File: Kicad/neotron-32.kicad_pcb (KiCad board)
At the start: 2 copper layers, 191.5 x 166.3 mm, 116 parts, among them J1001 2x3 Header, J1002 1x3 UART Debug Header, J1003 Double-mini-DIN-6, J1004 AVR-ISP-6, J101 Conn_02x06, J102 Conn_02x06, J103 Conn_02x04, J1101 DE9 Male, J1201 DE9 Male, J201 DIN-5 180 degree, J202 DIN-5 180 degree, J301 3.5mm Audio Jack TRS, J302 Conn_01x03_Male, J401 USB_B, J501 SD_Card, J601 Conn_02x13_Header, J801 DB15HD_Female, J901 Conn_02x05, SW1001 SW_Push_DPDT_ON_MO, SW401 SW_Push_DPDT_ON_MO, U1001 MCP23017_SP, U1002 ATmega328P-PU, U101 EK-TM4C123GXL, U201 74LS14, U202 6N138, U401 MIC2005A-2YM5, U402 TC1262-33, U601 MCP23S17_SP, U701 MCP7940N-xP, U901 ICL3232CPZMAX, Y701 32,768 Hz

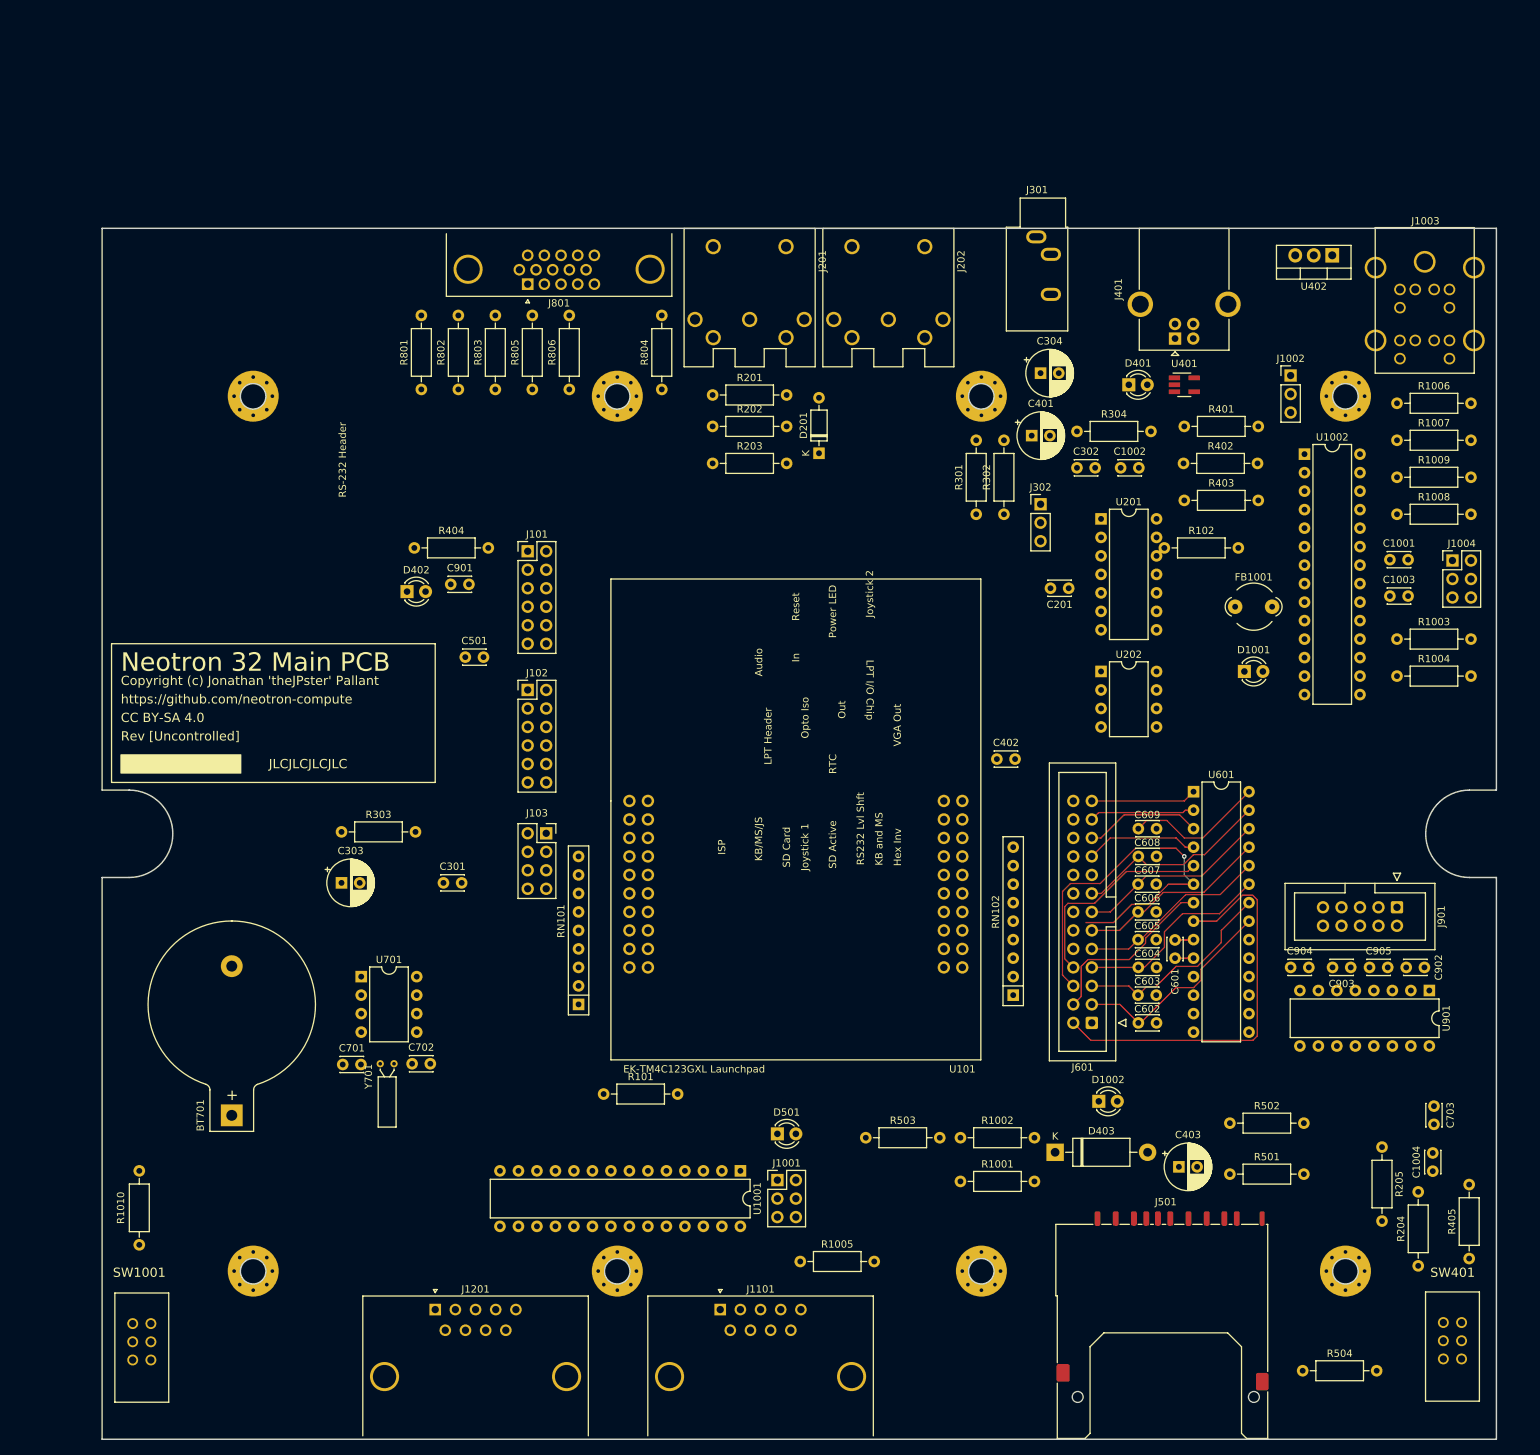
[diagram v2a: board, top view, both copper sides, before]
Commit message: Moved Joystick controller onto its own sheet.
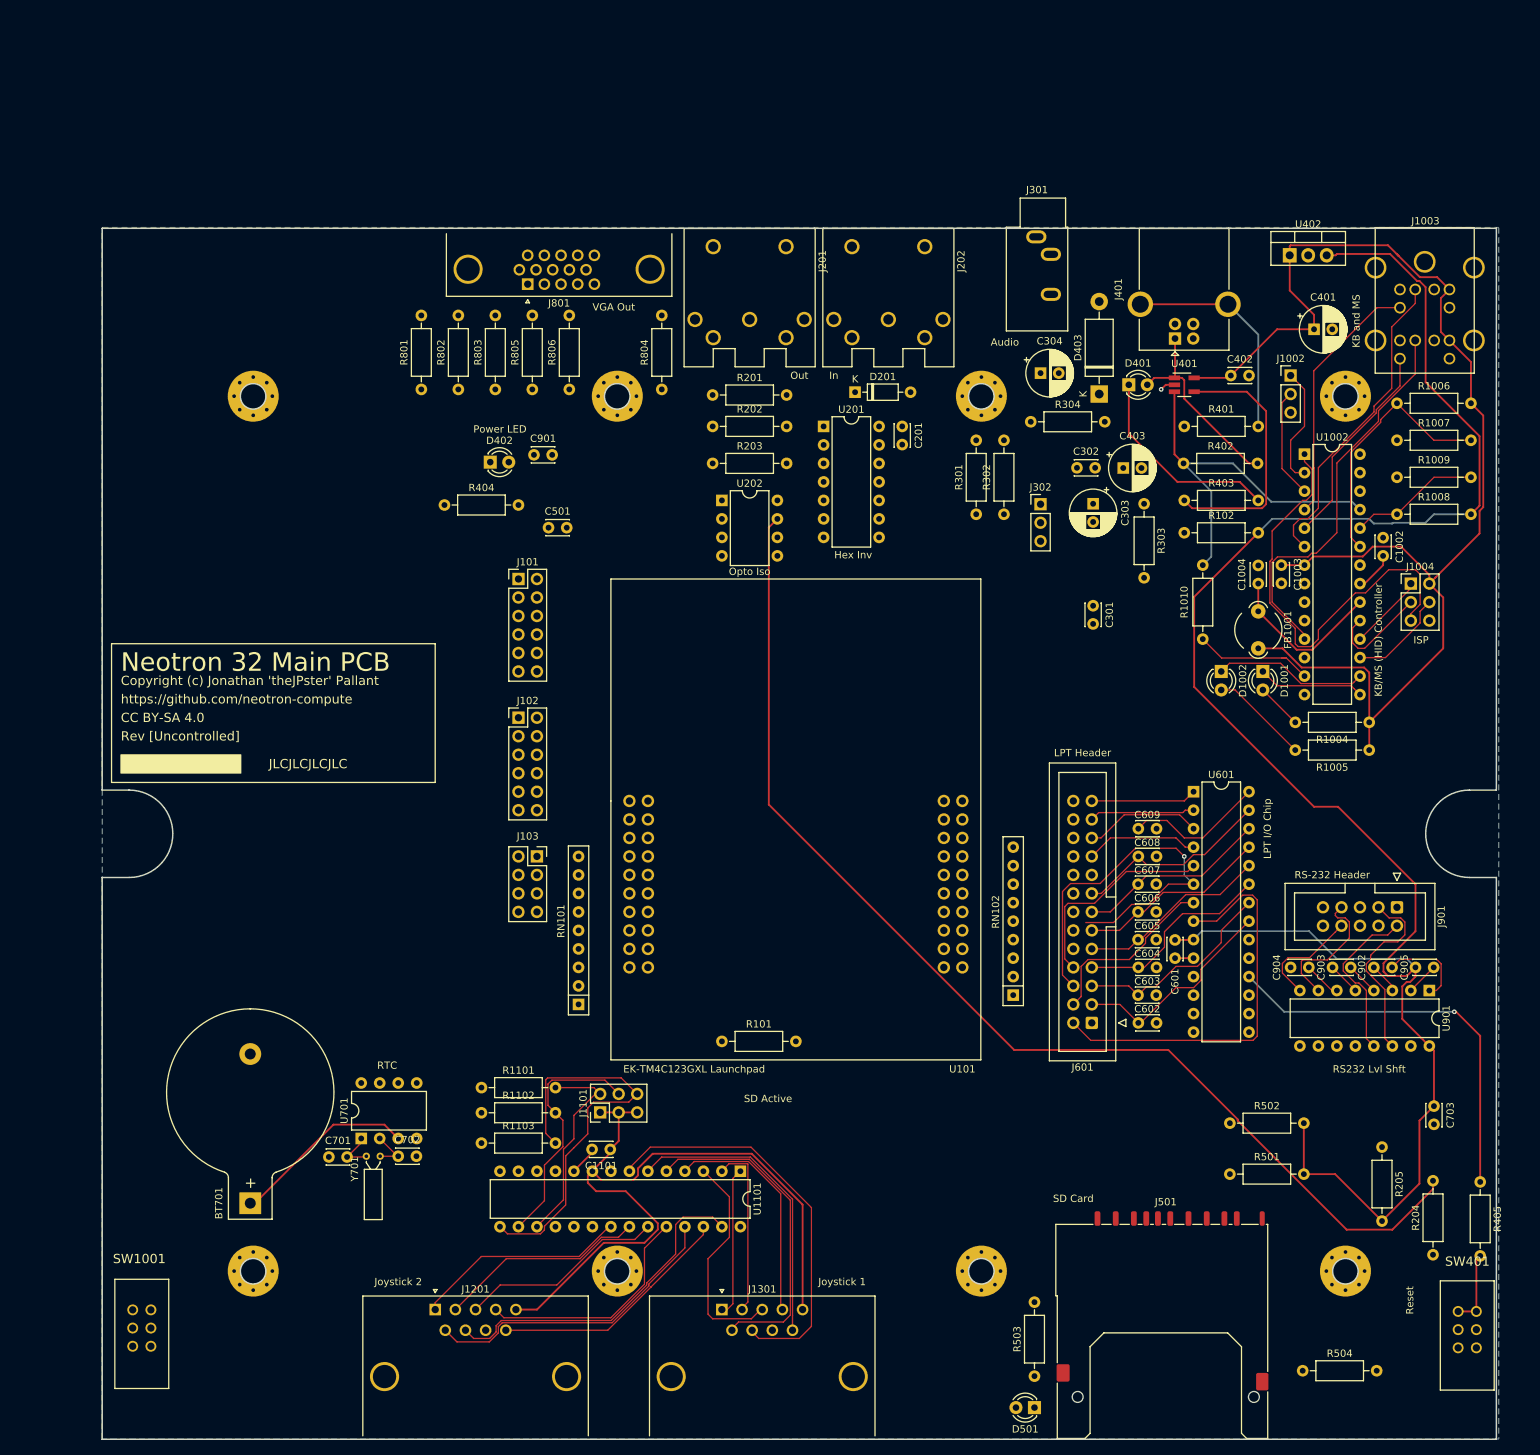
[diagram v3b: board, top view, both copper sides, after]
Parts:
- removed C1001: 100n, Capacitor_THT:C_Disc_D3.0mm_W2.0mm_P2.50mm
- removed J1001: 2x3 Header, Connector_PinHeader_2.54mm:PinHeader_2x03_P2.54mm_Vertical
- removed R1001, R1002, R1003: 10k, Resistor_THT:R_Axial_DIN0207_L6.3mm_D2.5mm_P10.16mm_Horizontal
- removed U1001: MCP23017_SP, Package_DIP:DIP-28_W7.62mm
- added C1101: 100n, Capacitor_THT:C_Disc_D3.0mm_W2.0mm_P2.50mm, F.Cu at (149.9, 173.6)
- added J1301: DE9 Male, Connector_Dsub:DSUB-9_Male_Horizontal_P2.77x2.84mm_EdgePinOffset14.56mm_Housed_MountingHolesOffset8.20mm, F.Cu at (165.2, 195.6)
- added R1101: 10k, Resistor_THT:R_Axial_DIN0207_L6.3mm_D2.5mm_P10.16mm_Horizontal, F.Cu at (132.2, 165.1)
- added R1102: 10k, Resistor_THT:R_Axial_DIN0207_L6.3mm_D2.5mm_P10.16mm_Horizontal, F.Cu at (132.2, 168.6)
- added R1103: 10k, Resistor_THT:R_Axial_DIN0207_L6.3mm_D2.5mm_P10.16mm_Horizontal, F.Cu at (132.2, 172.7)
- added U1101: MCP23017_SP, Package_DIP:DIP-28_W7.62mm, F.Cu at (167.8, 176.6)
- J1101: value DE9 Male -> 2x3 Header; footprint Connector_Dsub:DSUB-9_Male_Horizontal_P2.77x2.84mm_EdgePinOffset14.56mm_Housed_MountingHolesOffset8.20mm -> Connector_PinHeader_2.54mm:PinHeader_2x03_P2.54mm_Vertical
- moved R1010 168.1 mm to (231.3, 93.4)
- moved R303 119.1 mm to (223.2, 84.9), turned to 270 degrees
- moved C303 115.6 mm to (216.2, 84.9), turned to 270 degrees
- moved R1005 105.1 mm to (254.1, 118.8), turned to 180 degrees
- moved D403 104.3 mm to (217.1, 69.9), turned to 90 degrees
- moved C301 97.0 mm to (216.2, 98.9), turned to 270 degrees
- moved C403 96.3 mm to (220.4, 80.0)
- moved C1004 84.2 mm to (238.9, 95.9)
- moved C402 61.7 mm to (235.1, 67.3)
- moved D1002 61.4 mm to (233.8, 108.0), turned to 270 degrees
- moved U202 57.1 mm to (165.2, 84.5)
- moved D501 51.6 mm to (208.2, 209.1), turned to 180 degrees
- moved C401 41.4 mm to (246.6, 61.0)
- moved U201 40.2 mm to (179.2, 74.3)
- moved R503 40.1 mm to (208.2, 204.7), turned to 90 degrees
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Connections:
- net /Keyboard, Mouse and Joystick/AT_MISO renamed /Keyboard and Mouse/AT_MISO
- net /Keyboard, Mouse and Joystick/AT_MOSI renamed /Keyboard and Mouse/AT_MOSI
- net /Keyboard, Mouse and Joystick/AT_SCK renamed /Keyboard and Mouse/AT_SCK
- net /Keyboard, Mouse and Joystick/KB_CLK renamed /Keyboard and Mouse/KB_CLK
- net /Keyboard, Mouse and Joystick/KB_DAT renamed /Keyboard and Mouse/KB_DAT
- net /Keyboard, Mouse and Joystick/MON_3V3 renamed /Keyboard and Mouse/MON_3V3
- net /Keyboard, Mouse and Joystick/MON_5V0 renamed /Keyboard and Mouse/MON_5V0
- net /Keyboard, Mouse and Joystick/MS_CLK renamed /Keyboard and Mouse/MS_CLK
- net /Keyboard, Mouse and Joystick/MS_DAT renamed /Keyboard and Mouse/MS_DAT
- net /Keyboard, Mouse and Joystick/UART_RX renamed /Keyboard and Mouse/UART_RX
- net /Keyboard, Mouse and Joystick/UART_TX renamed /Keyboard and Mouse/UART_TX
- net /Keyboard, Mouse and Joystick/~AT_RESET renamed /Keyboard and Mouse/~AT_RESET
- J1101 pad 1: /Keyboard, Mouse and Joystick/JS1_UP -> +5V
- J1101 pad 2: /Keyboard, Mouse and Joystick/JS1_DOWN -> Net-(J1101-Pad2)
- J1101 pad 3: /Keyboard, Mouse and Joystick/JS1_LEFT -> +5V
- J1101 pad 4: /Keyboard, Mouse and Joystick/JS1_RIGHT -> Net-(J1101-Pad4)
- J1101 pad 6: /Keyboard, Mouse and Joystick/JS1_A_B -> Net-(J1101-Pad6)
- J1201 pad 1: /Keyboard, Mouse and Joystick/JS2_UP -> /Joystick/JS2_UP
- J1201 pad 2: /Keyboard, Mouse and Joystick/JS2_DOWN -> /Joystick/JS2_DOWN
- J1201 pad 3: /Keyboard, Mouse and Joystick/JS2_LEFT -> /Joystick/JS2_LEFT
- J1201 pad 4: /Keyboard, Mouse and Joystick/JS2_RIGHT -> /Joystick/JS2_RIGHT
- J1201 pad 6: /Keyboard, Mouse and Joystick/JS2_A_B -> /Joystick/JS2_A_B
- J1201 pad 7: /Keyboard, Mouse and Joystick/JS2_SELECT -> /Joystick/JS2_SELECT
- J1201 pad 9: /Keyboard, Mouse and Joystick/JS2_START_C -> /Joystick/JS2_START_C
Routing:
- net +5V: track 0.00 -> 280.8 mm
- net +3V3: track 2.56 -> 263.1 mm
- net Net-(R204-Pad2): track 0.00 -> 158.7 mm
- net /Keyboard and Mouse/~AT_RESET: track 0.00 -> 60.2 mm
- net Net-(J1101-Pad6): track 0.00 -> 56.7 mm
- net /Joystick/JS1_SELECT: track 0.00 -> 55.8 mm
- net /~RESET: track 0.00 -> 55.2 mm, vias 0 -> 1
- net /Keyboard and Mouse/MS_DAT: track 0.00 -> 53.8 mm
- net /~POWER_ON: track 0.00 -> 53.3 mm
- net /Joystick/JS2_SELECT: track 0.00 -> 46.2 mm
- net /Joystick/JS1_A_B: track 0.00 -> 44.9 mm
- net /Keyboard and Mouse/KB_DAT: track 0.00 -> 43.5 mm
- net /Joystick/JS2_A_B: track 0.00 -> 42.5 mm
- net /Joystick/JS1_START_C: track 0.00 -> 41.1 mm
- net Net-(R403-Pad1): track 0.00 -> 35.7 mm
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- added copper zone on B.Cu, net GND
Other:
- board text added: "KB/MS (HID) Controller"
- board text removed: "KB/MS/JS"
